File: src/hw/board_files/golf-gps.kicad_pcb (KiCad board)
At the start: 4 copper layers, 60.4 x 88.2 mm, 70 parts, among them J1 Conn_01x04_Pin, J2 Micro_SD_Card, P1 USB_C_Plug_USB2.0, SW1 SW_SPDT, SW2 BOOT, SW3 BTN_1, SW4 BTN_2, SW5 BTN_3, U1 MCP73831-2-OT, U2 TPS63031DSKR, U3 STM32L432KCU6, U4 NEO-M9N, Y1 32.768kHz

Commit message: Started filling out BOM
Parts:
- AE1: value Antenna -> ANT-GNSSCP-SM12L1
- D2: renamed from D4; footprint LED_SMD:LED_0805_2012Metric -> LED_SMD:LED_0603_1608Metric
- D5: footprint LED_SMD:LED_0805_2012Metric -> LED_SMD:LED_0603_1608Metric
- U2: renamed from U1; value MCP73831-2-OT -> MCP73831T-2ACI/OT
- renumbered C7 to C1, C17 to C10, C9 to C11, C18 to C12, C10 to C13, C11 to C14, C12 to C16, C13 to C17, C14 to C18, C3 to C2, C26 to C20, C20 to C24, C24 to C25, C25 to C26, C8 to C3, C1 to C6, C6 to C7, C2 to C8, C16 to C9, D2 to D1, D1 to D3, D3 to D4, J3 to J2, J2 to J3, R3 to R1, R13 to R10, R17 to R11, R14 to R12, R15 to R13, R10 to R14, R16 to R15, R4 to R2, R2 to R3, R1 to R4, R8 to R5, R9 to R6, R5 to R7, R6 to R8, R7 to R9, U2 to U1
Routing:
- net Net-(D5-A): track 1.90 -> 0.00 mm

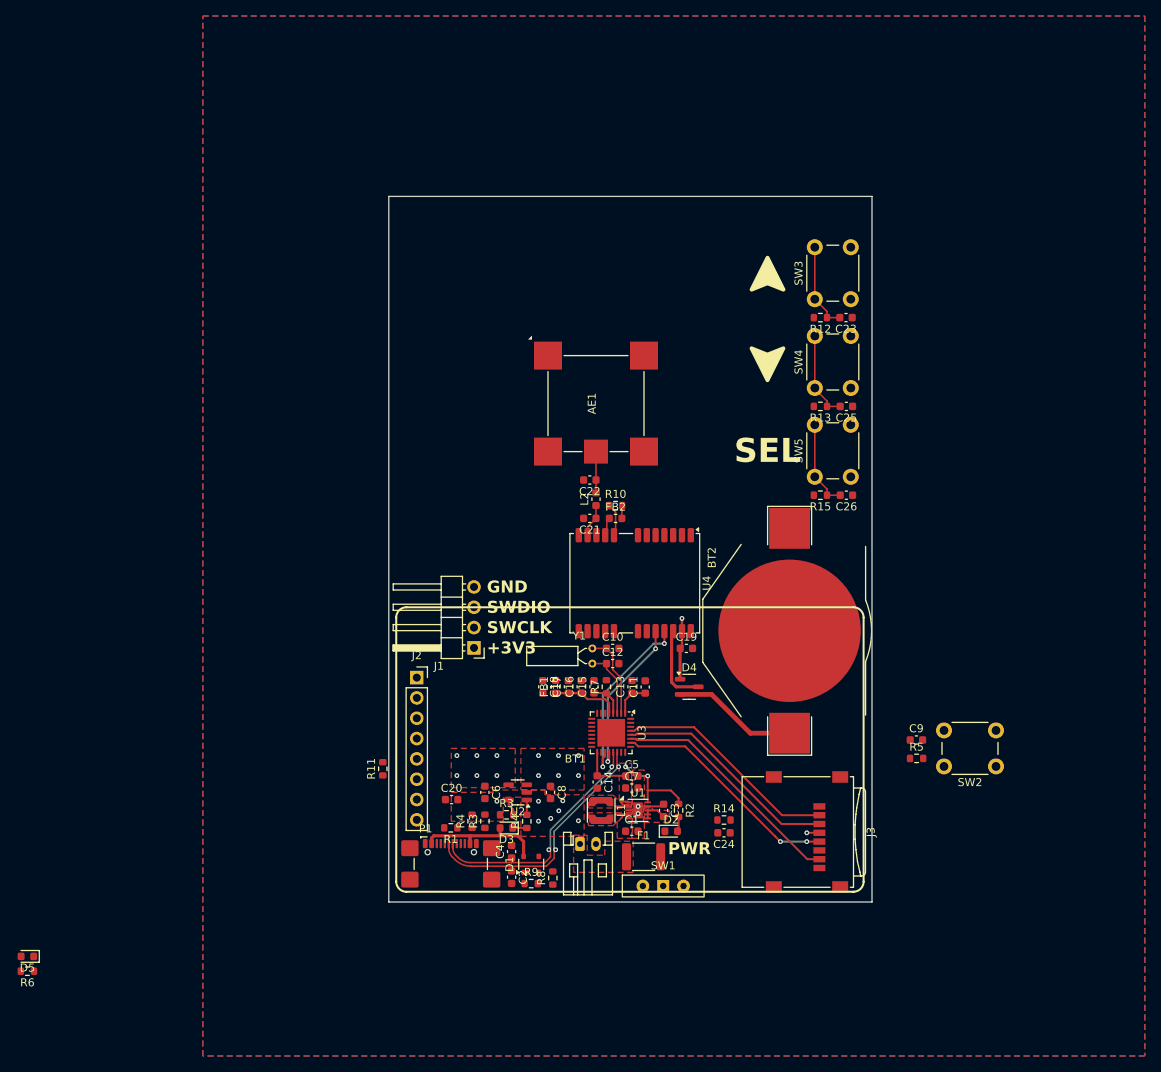
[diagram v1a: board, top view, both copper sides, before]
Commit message: PCB progress. Changed horizontal programming header to vertical.
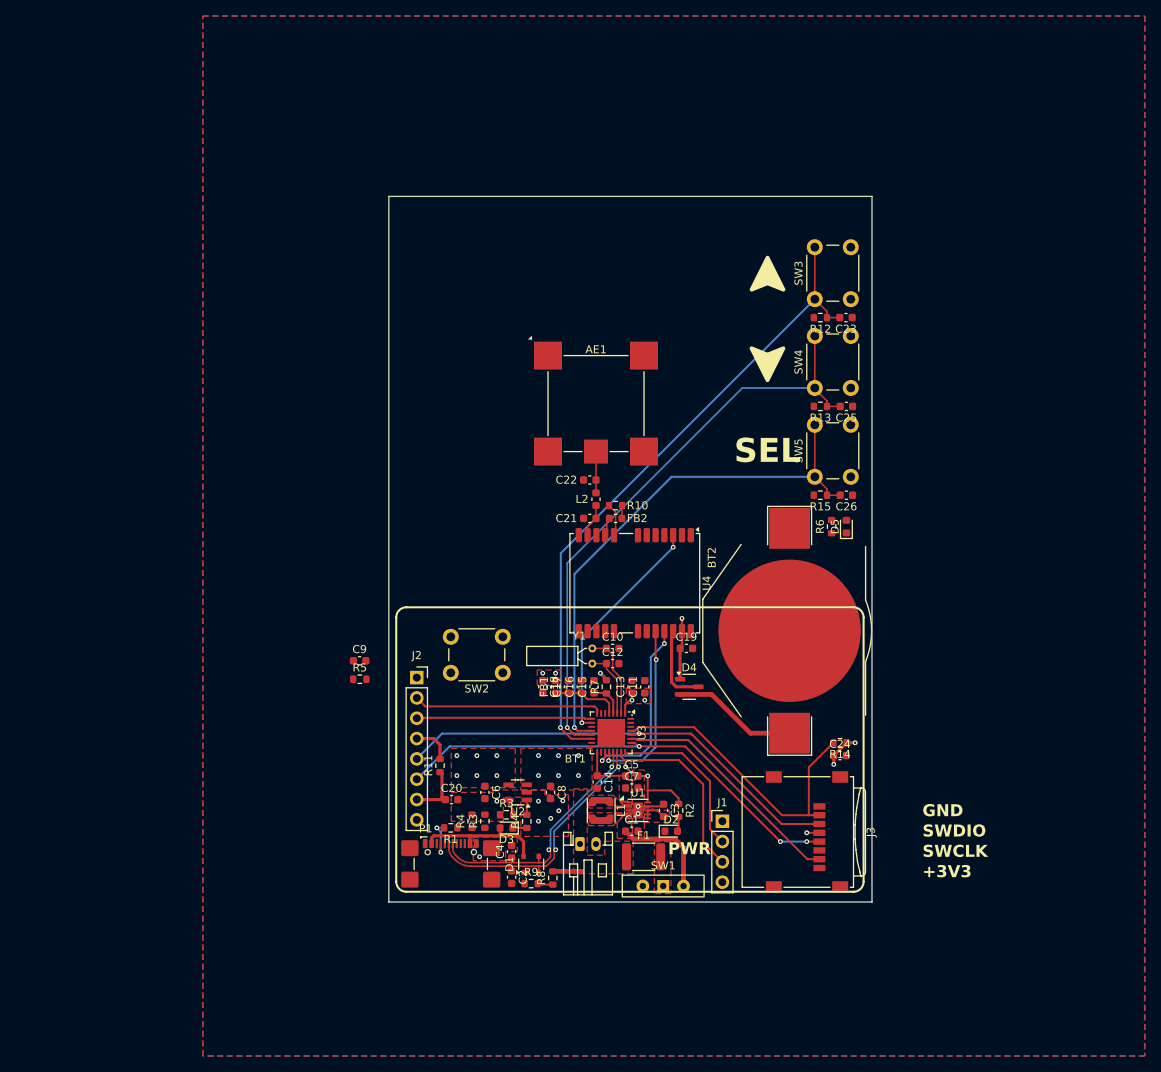
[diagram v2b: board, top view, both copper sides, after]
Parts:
- J1: footprint Connector_PinHeader_2.54mm:PinHeader_1x04_P2.54mm_Horizontal -> Connector_PinHeader_2.54mm:PinHeader_1x04_P2.54mm_Vertical
- moved D5 115.6 mm to (167.1, 107.7), turned to 90 degrees
- moved R6 114.9 mm to (165.2, 107.7), turned to 90 degrees
- moved C9 70.3 mm to (106.2, 124.5)
- moved R5 70.3 mm to (106.3, 126.8)
- moved SW2 62.8 mm to (124.2, 126.0)
- moved J1 37.9 mm to (151.6, 144.6), turned to 0 degrees
- moved C24 17.4 mm to (166.3, 136.3), turned to 0 degrees
- moved R14 17.4 mm to (166.3, 134.8), turned to 180 degrees
- moved R11 7.16 mm to (116.3, 137.6)
- moved C11 0.06 mm to (141.9, 127.8)
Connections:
- J2 pad 1: Net-(J2-BL) -> +3V3
- J2 pad 4: Net-(J2-BL) -> Net-(J2-RES)
- R11 pad 2: Net-(J2-BL) -> Net-(J2-RES)
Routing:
- net /Microcontroller/BTN_1: track 11.0 -> 82.3 mm, vias 0 -> 1
- net /Microcontroller/BTN_2: track 11.1 -> 75.1 mm, vias 0 -> 1
- net /Microcontroller/BTN_3: track 11.1 -> 67.7 mm, vias 0 -> 1
- net /Microcontroller/SPI3_SCK: track 28.7 -> 58.2 mm, vias 2 -> 3
- net /Microcontroller/GPS_PPS: track 0.00 -> 29.4 mm, vias 0 -> 2
- net /Microcontroller/SPI3_MOSI: track 28.3 -> 57.4 mm, vias 0 -> 1
- net /Microcontroller/LCD_CS: track 0.00 -> 23.6 mm
- net /Microcontroller/SWDIO: track 0.00 -> 22.9 mm
- net /Microcontroller/LCD_DC: track 0.00 -> 21.9 mm
- net /Microcontroller/SWCLK: track 0.00 -> 20.1 mm
- net Net-(SW1-A): track 0.00 -> 12.9 mm
- net +3V3: track 34.6 -> 45.7 mm, vias 4 -> 11
- net /Microcontroller/SD_CS: track 28.3 -> 38.7 mm
- net Net-(P1-CC): track 0.00 -> 5.30 mm, vias 0 -> 2
- net Net-(J2-RES): track 0.00 -> 5.00 mm
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- added copper zone on F.Cu, net Net-(SW1-B)
